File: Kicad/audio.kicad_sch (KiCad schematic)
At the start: 70 parts, among them J601 CD Audio In, J602 AC'97 Audio Header, J603 Line Out, U601 TLV320AIC23BPW, U602 STX-4335-5BGP-S1, Y601 12M 20pF

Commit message: Update schematic files to Kicad 6.
Had to fix some symbols which didn't have perfect matches in K6.
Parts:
- C16020: renamed from C620; symbol Neotron-Common-Hardware-rescue:CP_Small-Device -> Device:C_Polarized_Small
- C16021: renamed from C621; symbol Neotron-Common-Hardware-rescue:CP_Small-Device -> Device:C_Polarized_Small
- FB16001: renamed from FB601; symbol Neotron-Common-Hardware-rescue:Ferrite_Bead_Small-Device -> Device:FerriteBead_Small
- FB16002: renamed from FB602; symbol Neotron-Common-Hardware-rescue:Ferrite_Bead_Small-Device -> Device:FerriteBead_Small
- FB16003: renamed from FB603; symbol Neotron-Common-Hardware-rescue:Ferrite_Bead_Small-Device -> Device:FerriteBead_Small
- FB16004: renamed from FB604; symbol Neotron-Common-Hardware-rescue:Ferrite_Bead_Small-Device -> Device:FerriteBead_Small
- FB16005: renamed from FB605; symbol Neotron-Common-Hardware-rescue:Ferrite_Bead_Small-Device -> Device:FerriteBead_Small
- FB16006: renamed from FB606; symbol Neotron-Common-Hardware-rescue:Ferrite_Bead_Small-Device -> Device:FerriteBead_Small
- FB16007: renamed from FB607; symbol Neotron-Common-Hardware-rescue:Ferrite_Bead_Small-Device -> Device:FerriteBead_Small
- FB16008: renamed from FB608; symbol Neotron-Common-Hardware-rescue:Ferrite_Bead_Small-Device -> Device:FerriteBead_Small
- FB16009: renamed from FB609; symbol Neotron-Common-Hardware-rescue:Ferrite_Bead_Small-Device -> Device:FerriteBead_Small
- FB16010: renamed from FB610; symbol Neotron-Common-Hardware-rescue:Ferrite_Bead_Small-Device -> Device:FerriteBead_Small
- renumbered C601 to C16001, C602 to C16002, C603 to C16003, C604 to C16004, C605 to C16005, C606 to C16006, C607 to C16007, C608 to C16008, C609 to C16009, C610 to C16010, C611 to C16011, C612 to C16012, C613 to C16013, C614 to C16014, C615 to C16015, C616 to C16016, C617 to C16017, C618 to C16018, C619 to C16019, C622 to C16022, C623 to C16023, C624 to C16024, C625 to C16025, C626 to C16026, C627 to C16027, C628 to C16028, C629 to C16029, C630 to C16030, C631 to C16031, C632 to C16032, C633 to C16033, C634 to C16034, C635 to C16035, C636 to C16036, C637 to C16037, C638 to C16038, J601 to J16001, J602 to J16002, J603 to J16003, R601 to R16001, R602 to R16002, R603 to R16003, R604 to R16004, R605 to R16005, R606 to R16006, R607 to R16007, R608 to R16008, R609 to R16009, R610 to R16010, R611 to R16011, R612 to R16012, R613 to R16013, R614 to R16014, R615 to R16015, R616 to R16016, U601 to U16001, U602 to U16002, Y601 to Y16001

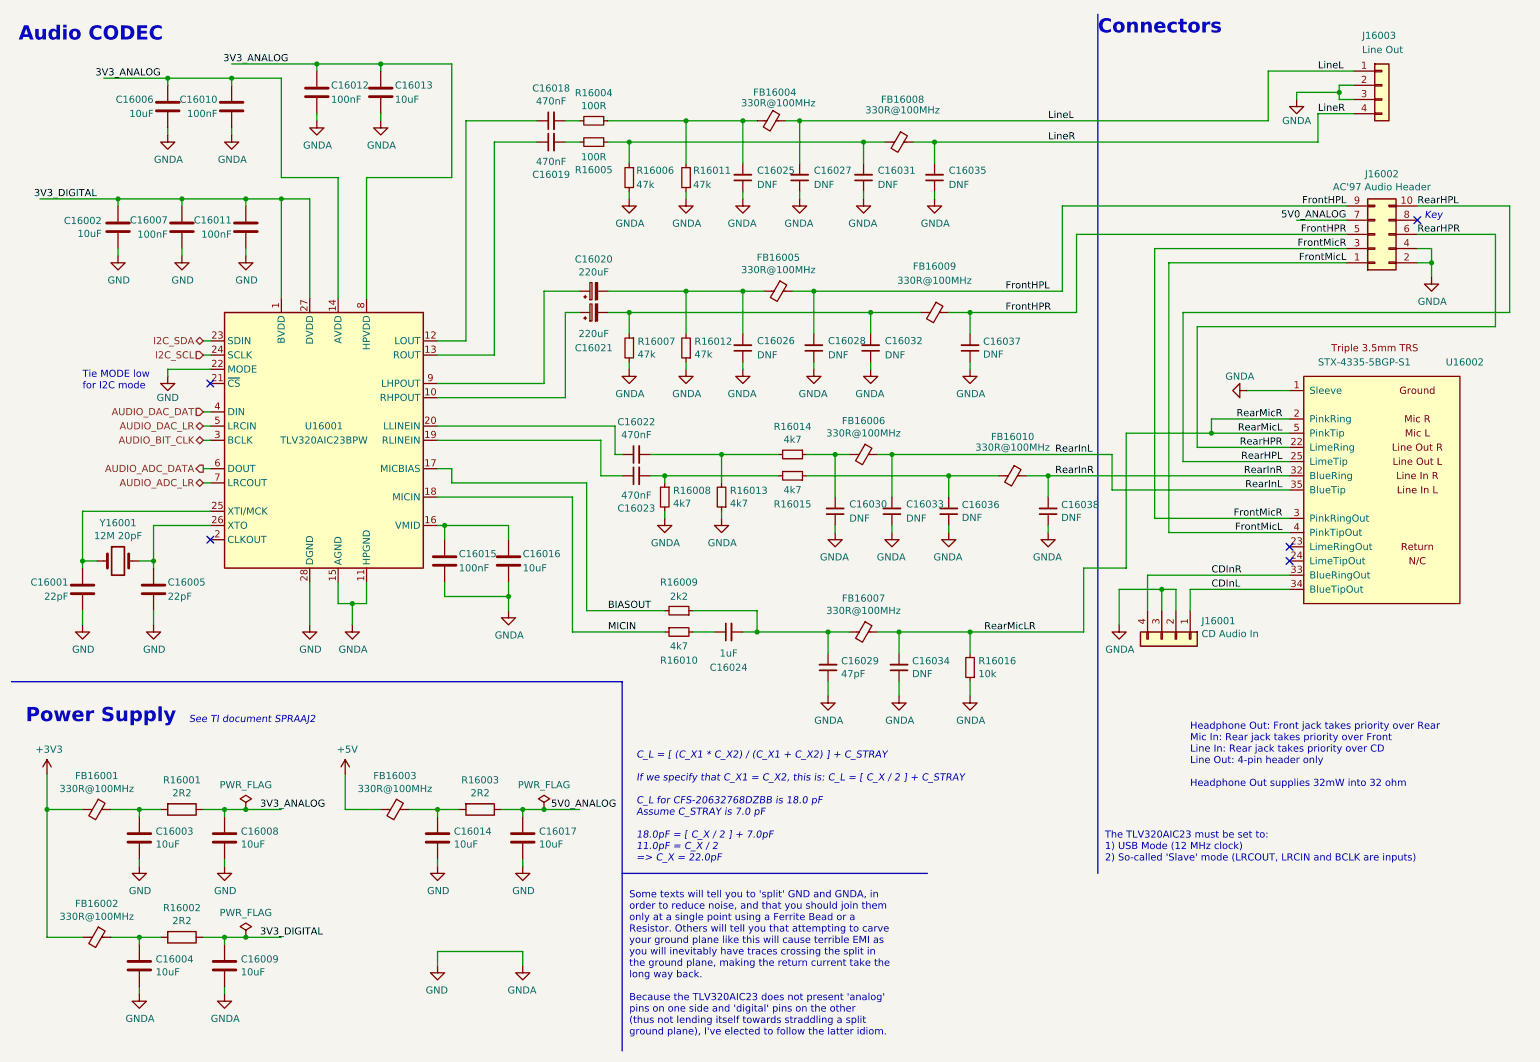
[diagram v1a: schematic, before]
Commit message: Imported sheets from Neotron Pico.
Standardised on +3V3 not +3.3V
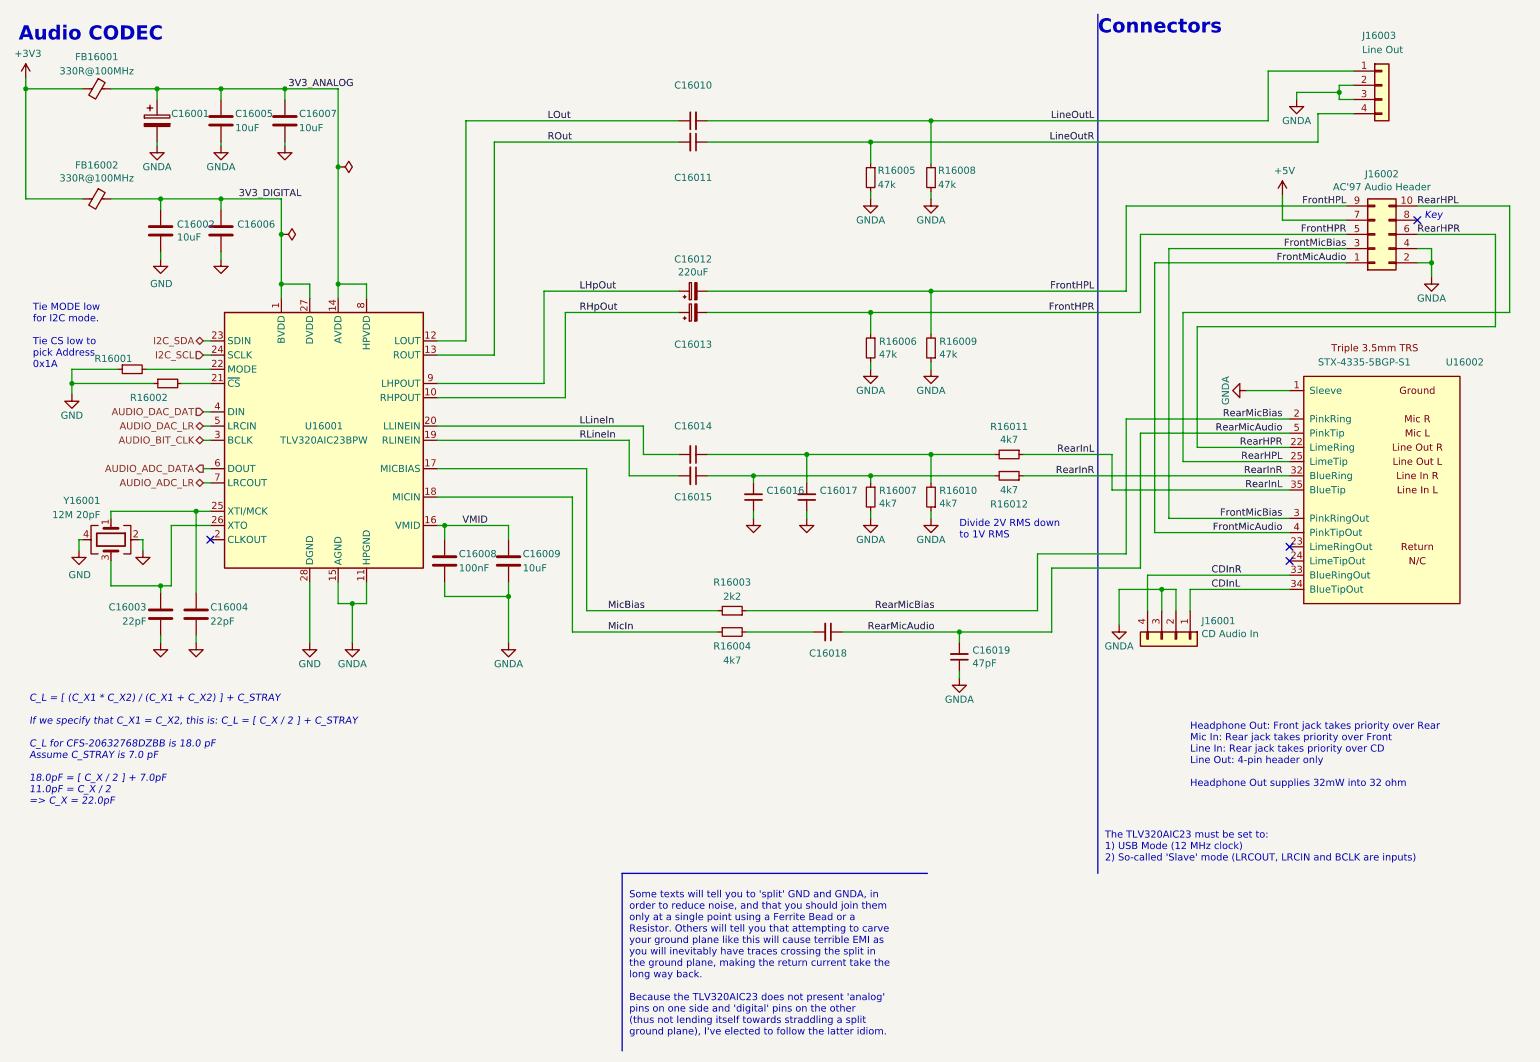
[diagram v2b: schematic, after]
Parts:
- removed C16003, C16004, C16008, C16009, C16014, C16017: 10uF, Capacitor_SMD:C_0805_2012Metric_Pad1.18x1.45mm_HandSolder, symbol Device:C
- removed C16007, C16010, C16011, C16012: 100nF, Capacitor_SMD:C_0805_2012Metric_Pad1.18x1.45mm_HandSolder, symbol Device:C
- removed C16019, C16022, C16023: 470nF, Capacitor_SMD:C_0805_2012Metric_Pad1.18x1.45mm_HandSolder, symbol Device:C_Small
- removed C16021: 220uF, Capacitor_THT:CP_Radial_D8.0mm_P5.00mm, symbol Device:C_Polarized_Small
- removed C16024: 1uF, Capacitor_SMD:C_0805_2012Metric_Pad1.18x1.45mm_HandSolder, symbol Device:C_Small
- removed C16025, C16026, C16027, C16028, C16030, C16031, C16032, C16033, C16034, C16035, C16036, C16037, C16038: DNF, Capacitor_SMD:C_0805_2012Metric_Pad1.18x1.45mm_HandSolder, symbol Device:C_Small
- removed FB16003, FB16004, FB16005, FB16006, FB16007, FB16008, FB16009, FB16010: 330R@100MHz, Inductor_SMD:L_0805_2012Metric_Pad1.15x1.40mm_HandSolder, symbol Device:FerriteBead_Small
- removed R16001, R16002, R16003: 2R2, Resistor_SMD:R_0805_2012Metric_Pad1.20x1.40mm_HandSolder, symbol Device:R
- removed R16004, R16005: 100R, Resistor_SMD:R_0805_2012Metric_Pad1.20x1.40mm_HandSolder, symbol Device:R_Small
- removed R16016: 10k, Resistor_SMD:R_0805_2012Metric_Pad1.20x1.40mm_HandSolder, symbol Device:R_Small
- added C16001: (no value), symbol Device:C_Polarized
- added C16006: (no value), symbol Device:C
- added C16010, C16011, C16014, C16015, C16016, C16017: (no value), symbol Device:C_Small
- added C16013: (no value), symbol Device:C_Polarized_Small
- added R16001, R16002: (no value), symbol Device:R_Small
- C16002: JLCPCB Collection (none) -> Basic; MPN CPL-CAP-X5R-0805-10UF-16V -> CL21A106KAYNNNE; Manufacturer CPL -> Samsung; Voltage 10V -> 25V
- C16003: renamed from C16001; Digikey 1276-1047-1-ND -> (none); JLCPCB Collection (none) -> Basic; Voltage 16V -> 50V
- C16004: renamed from C16005; Digikey 1276-1047-1-ND -> (none); JLCPCB Collection (none) -> Basic; Voltage 16V -> 50V
- C16005: renamed from C16013; JLCPCB Collection (none) -> Basic; MPN CPL-CAP-X5R-0805-10UF-16V -> CL21A106KAYNNNE; Manufacturer CPL -> Samsung; Voltage 10V -> 25V
- C16007: renamed from C16006; JLCPCB Collection (none) -> Basic; MPN CPL-CAP-X5R-0805-10UF-16V -> CL21A106KAYNNNE; Manufacturer CPL -> Samsung; Voltage 10V -> 25V
- C16008: renamed from C16015; JLCPCB Collection (none) -> Basic; MPN CPL-CAP-X7R-0805-100NF-50V -> CC0805KRX7R9BB104; Manufacturer CPL -> Yageo; Tolerance X5R -> X7R; Voltage 10V -> 50V
- C16009: renamed from C16016; JLCPCB Collection (none) -> Basic; MPN CPL-CAP-X5R-0805-10UF-16V -> CL21A106KAYNNNE; Manufacturer CPL -> Samsung; Voltage 10V -> 25V
- C16012: renamed from C16020; Digikey (none) -> P5182-ND; MPN CPL-CAP-ALU-RAD-220UF-50V -> ECA-1HM101; Manufacturer CPL -> Panasonic; Mouser (none) -> 667-ECA-1HM101; Voltage 6.3V -> 50V
- C16018: value 470nF -> (none); footprint Capacitor_SMD:C_0805_2012Metric_Pad1.18x1.45mm_HandSolder -> (none); Digikey 445-173276-1-ND -> (none); JLCPCB Collection (none) -> Basic; LCSC Part# C13967 -> C28323; MPN CL21B474KBFNNNE -> CL21B105KBFNNNE; Manufacturer TDK -> Samsung; Mouser 810-FG18X7R1H474KRT6 -> (none); Tolerance X5R -> X7R; Voltage 6.3V -> 50V
- C16019: renamed from C16029; Digikey 1276-1156-1-ND -> (none); JLCPCB Collection (none) -> Basic; Voltage 6.3V -> 50V
- FB16001, FB16002: JLCPCB Collection (none) -> Basic; MPN CPL-IND-FER-330OHM-1.5A -> GZ2012D601TF; Manufacturer CPL -> Sunlord; Tolerance 1.5A -> 25%
- J16001, J16002, J16003: DNP 1 -> 0
- R16003: renamed from R16009; Digikey RMCF0805FT2K20-ND -> (none); JLCPCB Collection (none) -> Basic; LCSC Part# C17520 -> C17604; MPN RMCF0805FT2K20 -> 0805W8F2001T5E; Manufacturer Stackpole -> Uniroyal
- R16004: renamed from R16010; JLCPCB Collection (none) -> Basic; LCSC Part# C17673 -> C17477; MPN CPL-RES-0805-4.7K-0.125W -> 0805W8F0000T5E; Manufacturer CPL -> Uniroyal
- R16005: renamed from R16006; Digikey RMCF0805FT47K5-ND -> (none); JLCPCB Collection (none) -> Basic; LCSC Part# C17713 -> C149504; MPN RMCF0805FT47K5 -> 0805W8F1003T5E; Manufacturer Stackpole -> Uniroyal
- R16006: renamed from R16007; Digikey RMCF0805FT47K5-ND -> (none); JLCPCB Collection (none) -> Basic; LCSC Part# C17713 -> C149504; MPN RMCF0805FT47K5 -> 0805W8F1003T5E; Manufacturer Stackpole -> Uniroyal
- R16007: renamed from R16008; JLCPCB Collection (none) -> Basic; MPN CPL-RES-0805-4.7K-0.125W -> 0805W8F4701T5E; Manufacturer CPL -> Uniroyal
- R16008: renamed from R16011; Digikey RMCF0805FT47K5-ND -> (none); JLCPCB Collection (none) -> Basic; LCSC Part# C17713 -> C149504; MPN RMCF0805FT47K5 -> 0805W8F1003T5E; Manufacturer Stackpole -> Uniroyal
- R16009: renamed from R16012; Digikey RMCF0805FT47K5-ND -> (none); JLCPCB Collection (none) -> Basic; LCSC Part# C17713 -> C149504; MPN RMCF0805FT47K5 -> 0805W8F1003T5E; Manufacturer Stackpole -> Uniroyal
- R16010: renamed from R16013; JLCPCB Collection (none) -> Basic; MPN CPL-RES-0805-4.7K-0.125W -> 0805W8F4701T5E; Manufacturer CPL -> Uniroyal
- R16011: renamed from R16014; JLCPCB Collection (none) -> Basic; MPN CPL-RES-0805-4.7K-0.125W -> 0805W8F4701T5E; Manufacturer CPL -> Uniroyal
- R16012: renamed from R16015; JLCPCB Collection (none) -> Basic; MPN CPL-RES-0805-4.7K-0.125W -> 0805W8F4701T5E; Manufacturer CPL -> Uniroyal
- U16001: Digikey 296-26817-1-ND -> (none); JLCPCB Collection (none) -> Extended; Mouser 595-TLV320AIC23BPW -> (none)
- Y16001: symbol Device:Crystal -> Device:Crystal_GND24; JLCPCB Collection (none) -> Basic; LCSC Part# C90883 -> C9002; MPN CPL-OSC-CRY-12MHZ-18PF -> X322512MSB4SI; Manufacturer CPL -> Yangxing Tech
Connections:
- net 5V0_ANALOG is gone; now on net +5V: J16002.7 (Pin_7)
- net LineL is gone; now on net LineOutL: J16003.1 (Pin_1)
- net LineR is gone; now on net LineOutR: J16003.4 (Pin_4)
- net 3V3_ANALOG: now also FB16001.1, C16001.1
- net 3V3_DIGITAL: now also FB16002.1, C16006.1
- net FrontHPL: now also C16012.2, R16009.2
- net FrontHPR: now also R16006.1, C16013.2
- net GND: now also Y16001.2, Y16001.4, C16001.2, C16006.2, C16016.1, C16017.1, R16001.1, R16002.1; no longer U16001.22 (MODE)
- net RearInL: now also R16011.1
- net RearInR: now also R16012.1
- net RHpOut: now reaches U16001.10 (RHPOUT)
- net RHpOut: now also C16013.1
- net LOut: now reaches U16001.12 (LOUT)
- net LOut: now also C16010.1; no longer C16018.1
- net ROut: now reaches U16001.13 (ROUT)
- net ROut: now also C16011.2
- net VMID: now reaches C16008.1, C16009.1, U16001.16 (VMID)
- net RLineIn: now reaches U16001.19 (RLINEIN)
- net RLineIn: now also C16015.2
- net LLineIn: now reaches U16001.20 (LLINEIN)
- net LLineIn: now also C16014.2
- net at U16001.21 (~{CS}): now also R16002.2
- net at U16001.25 (XTI/MCK), Y16001.1: now also C16004.1; no longer C16003.2
- net LHpOut: now reaches C16012.1, U16001.9 (LHPOUT)
- net at C16018.2: now also R16004.2
- net LineOutL: now reaches R16008.2
- net LineOutL: now also C16010.2
- net LineOutR: now reaches R16005.1
- net LineOutR: now also C16011.1
- net at R16010.2, R16011.2: now also C16014.1, C16017.2
- net at R16007.1, R16012.2: now also C16015.1, C16016.2
- net RearMicAudio: now reaches C16019.2
- net RearMicAudio: now also C16018.1, U16002.5 (PinkTip); no longer R16003.1
- net BIASOUT renamed MicBias
- net FrontMicL renamed FrontMicAudio
- net FrontMicR renamed FrontMicBias
- net MICIN renamed MicIn
- net RearMicL renamed RearMicBias
- net RearMicBias: now also R16003.1; no longer U16002.5 (PinkTip)
- new net: R16001.2, U16001.22 (MODE)
- new net: C16003.2, U16001.26 (XTO), Y16001.3
- no-connect marks 5 -> 4
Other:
- note added: "Divide 2V RMS down to 1V RMS"
- note added: "Tie MODE low for I2C mode. Tie CS low to pick Address 0x1A"
- note removed: "Power Supply"
- note removed: "See TI document SPRAAJ2"
- note removed: "Tie MODE low for I2C mode"
- company: https://neotron-compute.github.io/ -> https://neotron-compute.github.io
- moved on the sheet: C16002, C16003, C16004, C16005, C16007, C16012, C16019, FB16001, FB16002, R16003, R16004, R16005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

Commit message: Set missing footprints and update PCB
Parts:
- C16001, C16013: value (none) -> 100u; footprint (none) -> Capacitor_THT:CP_Radial_D8.0mm_P5.00mm
- C16002, C16005, C16007, C16009: value 10uF -> 10u; JLCPCB Collection Basic -> (none); LCSC Part# C15850 -> (none); MPN CL21A106KAYNNNE -> (none); Manufacturer Samsung -> (none)
- C16003, C16004: value 22pF -> 22p
- C16006: value (none) -> 10u; footprint (none) -> Capacitor_SMD:C_0805_2012Metric_Pad1.18x1.45mm_HandSolder; JLCPCB Collection Basic -> (none); LCSC Part# C15850 -> (none); MPN CL21A106KAYNNNE -> (none); Manufacturer Samsung -> (none)
- C16008: value 100nF -> 100n
- C16010, C16011, C16014, C16015, C16018: value (none) -> 1u; footprint (none) -> Capacitor_SMD:C_0805_2012Metric_Pad1.18x1.45mm_HandSolder
- C16012: value 220uF -> 100u
- C16016, C16017: value (none) -> 47p; footprint (none) -> Capacitor_SMD:C_0805_2012Metric_Pad1.18x1.45mm_HandSolder
- C16019: value 47pF -> 47p
- R16001, R16002: value (none) -> 0R; footprint (none) -> Resistor_SMD:R_0805_2012Metric_Pad1.20x1.40mm_HandSolder

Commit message: Re-imported from Neotron Pico v1.1.
This time I deleted the sheets from the top level and then re-added pointing at the new files. I also reset the PCB dimensions to match the Neotron Pico.

This seems to have done a better job importing footprints.
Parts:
- C202: renamed from C16002; JLCPCB Collection (none) -> Basic; LCSC Part# (none) -> C15850; MPN (none) -> CL21A106KAYNNNE; Manufacturer (none) -> Samsung
- C205: renamed from C16005; JLCPCB Collection (none) -> Basic; LCSC Part# (none) -> C15850; MPN (none) -> CL21A106KAYNNNE; Manufacturer (none) -> Samsung
- C206: renamed from C16006; JLCPCB Collection (none) -> Basic; LCSC Part# (none) -> C15850; MPN (none) -> CL21A106KAYNNNE; Manufacturer (none) -> Samsung
- C207: renamed from C16007; JLCPCB Collection (none) -> Basic; LCSC Part# (none) -> C15850; MPN (none) -> CL21A106KAYNNNE; Manufacturer (none) -> Samsung
- C209: renamed from C16009; JLCPCB Collection (none) -> Basic; LCSC Part# (none) -> C15850; MPN (none) -> CL21A106KAYNNNE; Manufacturer (none) -> Samsung
- J201: renamed from J16001; value CD Audio In -> Conn_01x04
- J202: renamed from J16002; value AC'97 Audio Header -> Conn_02x05
- J203: renamed from J16003; value Line Out -> Conn_01x04
- R203: renamed from R16003; value 2k2 -> 2k
- R204: renamed from R16004; value 4k7 -> 0R
- R205: renamed from R16005; value 47k -> 100k
- R206: renamed from R16006; value 47k -> 100k
- R208: renamed from R16008; value 47k -> 100k
- R209: renamed from R16009; value 47k -> 100k
- Y201: renamed from Y16001; footprint Crystal:Crystal_SMD_5032-2Pin_5.0x3.2mm_HandSoldering -> Crystal:Crystal_SMD_3225-4Pin_3.2x2.5mm_HandSoldering
- renumbered C16001 to C201, C16003 to C203, C16004 to C204, C16008 to C208, C16010 to C210, C16011 to C211, C16012 to C212, C16013 to C213, C16014 to C214, C16015 to C215, C16016 to C216, C16017 to C217, C16018 to C218, C16019 to C219, FB16001 to FB201, FB16002 to FB202, R16001 to R201, R16002 to R202, R16007 to R207, R16010 to R210, R16011 to R211, R16012 to R212, U16001 to U201, U16002 to U202
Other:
- note added: "As built in Neotron Pico v1.1"
- company: https://neotron-compute.github.io -> https://neotron-compute.github.io/
